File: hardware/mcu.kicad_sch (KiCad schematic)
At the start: 94 parts, among them J10 PRPC006SAAN-RC, J11 PRPC004SAAN-RC, J12 SBH11-NBPC-D05-SM-BK, J13 PRPC006SAAN-RC, J14 PRPC001DAAN-RC, J15 PRPC006SAAN-RC, J16 PRPC006SAAN-RC, J17 PRPC006SAAN-RC, J18 PRPC006SAAN-RC, U6 MCP9808T-E/MC, U7 AT25SF081B-MAHB-T, U8 STM32L552CEU6, U9 TCA9554PW, Y1 ECS-160-9-37-CKM-TR3, Y2 ABS05-32.768KHZ-9-T

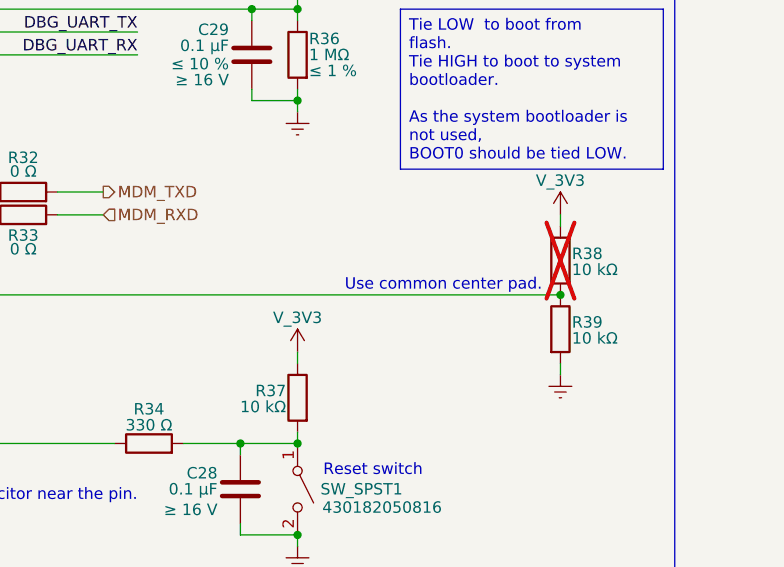
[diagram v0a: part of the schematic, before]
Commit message: HW: Increase pull-up on SIM_DET
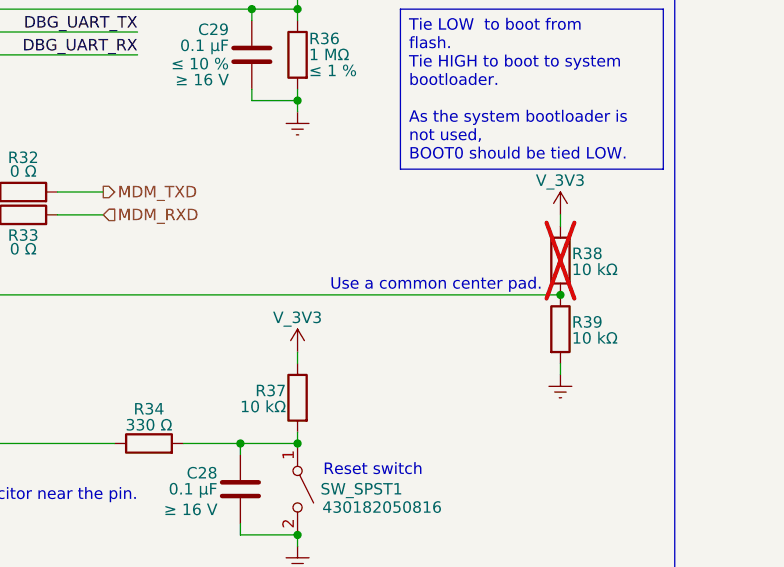
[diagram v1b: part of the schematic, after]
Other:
- note added: "Use a common center pad."
- note removed: "Use common center pad."
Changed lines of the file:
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@@
 		)
 	)
-	(text "Use common center pad."
+	(text "Use a common center pad."
 		(exclude_from_sim no)
 		(at 391.668 109.982 0)

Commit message: HW: Improve comments
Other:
- note added: "Place the GPIO headers along the edges of the PCB."
- note removed: "Place headers for GPIOs along the edges of the PCB."
- moved on the sheet: R38, R39
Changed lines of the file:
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@@
 	(text "Use a common center pad."
 		(exclude_from_sim no)
-		(at 391.668 109.982 0)
+		(at 368.808 108.712 0)
 		(effects
 			(font
@@
 		)
 	)
-	(text "Place headers for GPIOs along the edges of the PCB."
+	(text "Place the GPIO headers along the edges of the PCB."
 		(exclude_from_sim no)
 		(at 306.07 212.09 0)
@@
 		)
 	)
-	(text_box "V_BAT is at 4.2 V when fully charged.\nThis circuit draws at most\n4.2 V / 2 MΩ = 2.1 µA.\n\nV_BAT_SENSE is 2.1 V when fully charged and 1.75 V when almost empty."
+	(text_box "V_BAT is at 4.2 V when fully charged.\nThis circuit draws a maximum current of:\n4.2 V / 2 MΩ = 2.1 µA.\n\nV_BAT_SENSE is 2.1 V when fully charged and 1.75 V when nearly empty."
 		(exclude_from_sim no)
 		(at 330.2 52.07 0)
@@
 		)
 	)
-	(text_box "Tie LOW  to boot from flash.\nTie HIGH to boot to system bootloader.\n\nAs the system bootloader is not used,\nBOOT0 should be tied LOW."
+	(text_box "Connect LOW to boot from flash.\nConnect HIGH to boot to the system bootloader.\n\nSince the system bootloader is not used,\nBOOT0 should be connected to LOW."
 		(exclude_from_sim no)
-		(at 375.92 80.01 0)
-		(size 29.21 17.78)
+		(at 378.46 100.33 0)
+		(size 26.67 20.32)
 		(margins 0.9525 0.9525 0.9525 0.9525)
 		(stroke
@@
 	)
 	(junction
-		(at 393.7 111.76)
+		(at 370.84 110.49)
 		(diameter 0)
 		(color 0 0 0 0)
@@
 	(wire
 		(pts
-			(xy 393.7 120.65) (xy 393.7 119.38)
+			(xy 370.84 119.38) (xy 370.84 118.11)
 		)
 		(stroke
@@
 	(wire
 		(pts
-			(xy 393.7 102.87) (xy 393.7 104.14)
+			(xy 370.84 101.6) (xy 370.84 102.87)
 		)
 		(stroke
@@
 	(wire
 		(pts
-			(xy 330.2 111.76) (xy 393.7 111.76)
+			(xy 330.2 110.49) (xy 370.84 110.49)
 		)
 		(stroke
@@
 	(wire
 		(pts
-			(xy 330.2 111.76) (xy 330.2 125.73)
+			(xy 330.2 110.49) (xy 330.2 125.73)
 		)
 		(stroke
@@
 	(symbol
 		(lib_id "Device:R")
-		(at 393.7 115.57 0)
+		(at 370.84 114.3 0)
 		(unit 1)
 		(exclude_from_sim no)
@@
 		(dnp no)
 		(property "Reference" "R39"
-			(at 394.97 114.808 0)
+			(at 372.11 113.538 0)
 			(effects
 				(font
@@
 		)
 		(property "Value" "10 kΩ"
-			(at 394.97 116.586 0)
+			(at 372.11 115.316 0)
 			(effects
 				(font
@@
 		)
 		(property "Footprint" "Resistor_SMD:R_0402_1005Metric"
-			(at 391.922 115.57 90)
+			(at 369.062 114.3 90)
 			(effects
 				(font
@@
 		)
 		(property "Datasheet" "~"
-			(at 393.7 115.57 0)
+			(at 370.84 114.3 0)
 			(effects
 				(font
@@
 		)
 		(property "Description" ""
-			(at 393.7 115.57 0)
+			(at 370.84 114.3 0)
 			(effects
 				(font
@@
 		)
 		(property "Manufacturer" "Würth Elektronik"
-			(at 393.7 115.57 0)
+			(at 370.84 114.3 0)
 			(effects
 				(font
@@
 		)
 		(property "MPN" "560112110020"
-			(at 393.7 115.57 0)
+			(at 370.84 114.3 0)
 			(effects
 				(font
@@
 		)
 		(property "DigiKey Part Number" "732-560112110020CT-ND"
-			(at 393.7 115.57 0)
+			(at 370.84 114.3 0)
 			(effects
 				(font
@@
 		)
 		(property "Footprint review check" "+"
-			(at 393.7 115.57 0)
+			(at 370.84 114.3 0)
 			(effects
 				(font
@@
 		)
 		(property "Tolerance" "≤ 5 %"
-			(at 394.97 117.348 0)
+			(at 372.11 116.078 0)
 			(effects
 				(font
@@
 	(symbol
 		(lib_id "power:Earth")
-		(at 393.7 120.65 0)
+		(at 370.84 119.38 0)
 		(unit 1)
 		(exclude_from_sim no)
@@
 		(fields_autoplaced yes)
 		(property "Reference" "#PWR086"
-			(at 393.7 127 0)
+			(at 370.84 125.73 0)
 			(effects
 				(font
@@
 		)
 		(property "Value" "GND"
-			(at 393.7 125.73 0)
+			(at 370.84 124.46 0)
 			(effects
 				(font
@@
 		)
 		(property "Footprint" ""
-			(at 393.7 120.65 0)
+			(at 370.84 119.38 0)
 			(effects
 				(font
@@
 		)
 		(property "Datasheet" "~"
-			(at 393.7 120.65 0)
+			(at 370.84 119.38 0)
 			(effects
 				(font
@@
 		)
 		(property "Description" "Power symbol creates a global label with name \"Earth\""
-			(at 393.7 120.65 0)
+			(at 370.84 119.38 0)
 			(effects
 				(font
@@
 	(symbol
 		(lib_id "power:+3.3V")
-		(at 393.7 102.87 0)
+		(at 370.84 101.6 0)
 		(unit 1)
 		(exclude_from_sim no)
@@
 		(dnp no)
 		(property "Reference" "#PWR085"
-			(at 393.7 106.68 0)
+			(at 370.84 105.41 0)
 			(effects
 				(font
@@
 		)
 		(property "Value" "V_3V3"
-			(at 393.7 99.06 0)
+			(at 370.84 97.79 0)
 			(effects
 				(font
@@
 		)
 		(property "Footprint" ""
-			(at 393.7 102.87 0)
+			(at 370.84 101.6 0)
 			(effects
 				(font
@@
 		)
 		(property "Datasheet" ""
-			(at 393.7 102.87 0)
+			(at 370.84 101.6 0)
 			(effects
 				(font
@@
 		)
 		(property "Description" "Power symbol creates a global label with name \"+3.3V\""
-			(at 393.7 102.87 0)
+			(at 370.84 101.6 0)
 			(effects
 				(font
@@
 	(symbol
 		(lib_id "Device:R")
-		(at 393.7 107.95 0)
+		(at 370.84 106.68 0)
 		(unit 1)
 		(exclude_from_sim no)
@@
 		(dnp yes)
 		(property "Reference" "R38"
-			(at 394.97 107.188 0)
+			(at 372.11 105.918 0)
 			(effects
 				(font
@@
 		)
 		(property "Value" "10 kΩ"
-			(at 394.97 108.966 0)
+			(at 372.11 107.696 0)
 			(effects
 				(font
@@
 		)
 		(property "Footprint" "Resistor_SMD:R_0402_1005Metric"
-			(at 391.922 107.95 90)
+			(at 369.062 106.68 90)
 			(effects
 				(font
@@
 		)
 		(property "Datasheet" "~"
-			(at 393.7 107.95 0)
+			(at 370.84 106.68 0)
 			(effects
 				(font
@@
 		)
 		(property "Description" ""
-			(at 393.7 107.95 0)
+			(at 370.84 106.68 0)
 			(effects
 				(font
@@
 		)
 		(property "Manufacturer" "Würth Elektronik"
-			(at 393.7 107.95 0)
+			(at 370.84 106.68 0)
 			(effects
 				(font
@@
 		)
 		(property "MPN" "560112110020"
-			(at 393.7 107.95 0)
+			(at 370.84 106.68 0)
 			(effects
 				(font
@@
 		)
 		(property "DigiKey Part Number" "732-560112110020CT-ND"
-			(at 393.7 107.95 0)
+			(at 370.84 106.68 0)
 			(effects
 				(font
@@
 		)
 		(property "Footprint review check" "+"
-			(at 393.7 107.95 0)
+			(at 370.84 106.68 0)
 			(effects
 				(font
@@
 		)
 		(property "Tolerance" "≤ 5 %"
-			(at 394.97 109.728 0)
+			(at 372.11 108.458 0)
 			(effects
 				(font

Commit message: HW: Add battery monitoring with MAX17048
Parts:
- removed C29: 0.1 µF, Capacitor_SMD:C_0402_1005Metric, symbol Device:C
- removed R30, R31: 0 Ω, Resistor_SMD:R_0402_1005Metric, symbol Device:R
- removed R35, R36: 1 MΩ, Resistor_SMD:R_0402_1005Metric, symbol Device:R
- removed TP21: TestPoint, TestPoint:TestPoint_Pad_D1.0mm, symbol Connector:TestPoint
- added R20: 10 kΩ, Resistor_SMD:R_0402_1005Metric, symbol Device:R
- added R24, R32, R33: 0 Ω, Resistor_SMD:R_0402_1005Metric, symbol Device:R
- renumbered C13 to C14, C14 to C15, C15 to C16, C16 to C17, C17 to C18, C18 to C19, C19 to C20, C20 to C21, C21 to C23, C23 to C24, C24 to C25, C25 to C26, C26 to C27, C27 to C28, C28 to C29, R22 to R18, R21 to R19, R18 to R21, R19 to R22, R20 to R23, R23 to R25, R24 to R26, R25 to R27, R26 to R28, R27 to R29, R28 to R30, R29 to R31, R32 to R34, R33 to R35, R34 to R36, TP20 to TP21, U9 to U10, U6 to U7, U7 to U8, U8 to U9
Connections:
- net V_BAT_SENSE is gone; now on net GPIO_PA1: U9.11 (PA1)
- net DBG_UART_RX: now also R33.2
- net DBG_UART_TX: now also R32.2
- net V_3V3: now also R20.1
- net GPIO_PA1: now reaches J18.5 (Pin_5)
- net at U9.12 (PA2): now also R32.1
- net at U9.13 (PA3): now also R33.1
- net at U10.12 (P7): now also R24.2
- new net BAT_INT: R20.2, R24.1
- no-connect marks 10 -> 8
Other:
- moved on the sheet: C23, R18, R19, R21, R22, R23, R38, R39, U10

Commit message: HW: Reorganize schematic
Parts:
- removed C15: 0.1 µF, Capacitor_SMD:C_0402_1005Metric, symbol Device:C
- removed C25, C26, C27, C28: 8 pF, Capacitor_SMD:C_0402_1005Metric, symbol Device:C
- removed J11: PRPC004SAAN-RC, Connector_PinHeader_2.54mm:PinHeader_1x04_P2.54mm_Vertical, symbol Connector_Generic:Conn_01x04
- removed J14: PRPC001DAAN-RC, Connector_PinHeader_2.54mm:PinHeader_1x02_P2.54mm_Vertical, symbol Connector_Generic:Conn_01x02
- removed LED6, LED7, LED8: 150141RS73100, LED_SMD:LED_PLCC_2835, symbol Device:LED
- removed R18: 4.7 kΩ, Resistor_SMD:R_0402_1005Metric, symbol Device:R
- removed R20: 10 kΩ, Resistor_SMD:R_0402_1005Metric, symbol Device:R
- removed R21, R22, R23, R24, R32, R33, R34, R35: 0 Ω, Resistor_SMD:R_0402_1005Metric, symbol Device:R
- removed R25: 2.2 kΩ, Resistor_SMD:R_0402_1005Metric, symbol Device:R
- removed TP22, TP23, TP24, TP25, TP26, TP27, TP28, TP29, TP30, TP31, TP32, TP33, TP34, TP35, TP36, TP37, TP38, TP39, TP40, TP41, TP42, TP43, TP44, TP45, TP46, TP47, TP48, TP49: TestPoint, TestPoint:TestPoint_Pad_D1.0mm, symbol Connector:TestPoint
- removed U10: TCA9554PW, Package_SO:TSSOP-16_4.4x5mm_P0.65mm, symbol Interface_Expansion:TCA9554PW
- removed U7: MCP9808T-E/MC, Package_DFN_QFN:DFN-8-1EP_3x2mm_P0.5mm_EP1.75x1.45mm, symbol MCP9808:MCP9808T-E/MC
- added C18, C19, C24: 8 pF, Capacitor_SMD:C_0402_1005Metric, symbol Device:C
- added J16: PRPC006SAAN-RC, Connector_PinHeader_2.54mm:PinHeader_1x06_P2.54mm_Vertical, symbol Connector_Generic:Conn_01x06
- added J18: PRPC001DAAN-RC, Connector_PinHeader_2.54mm:PinHeader_1x02_P2.54mm_Vertical, symbol Connector_Generic:Conn_01x02
- added R28, R29: 0 Ω, Resistor_SMD:R_0402_1005Metric, symbol Device:R
- added R31: 4.7 kΩ, Resistor_SMD:R_0402_1005Metric, symbol Device:R
- C23: value 0.1 µF -> 8 pF; Class X7R -> C0G; DigiKey Part Number 490-7998-1-ND -> 490-3109-1-ND; MPN GCM155R71C104KA55J -> GJM1555C1H8R0CB01D; Tolerance ≤ 10 % -> ≤ 1 %; Voltage ≥ 16 V -> ≥ 10 V
- R26, R27: value 2.2 kΩ -> 0 Ω; DigiKey Part Number 732-560112110087CT-ND -> 732-560112110001CT-ND; MPN 560112110087 -> 560112110001; Size (none) -> 0402; Tolerance ≤ 5 % -> (none)
- U7: renamed from U9; Digi-Key Part Number (none) -> 497-STM32L552CEU6-ND
- renumbered C29 to C14, C16 to C15, C17 to C16, C18 to C17, C19 to C20, C20 to C21, C21 to C22, C22 to C25, C24 to C26, C14 to C27, J13 to J10, J12 to J11, J15 to J12, J16 to J13, J17 to J14, J18 to J15, J10 to J17, R30 to R18, R31 to R19, R28 to R20, R29 to R21, R37 to R22, R38 to R23, R39 to R24, R36 to R25, R19 to R30
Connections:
- net LED_B is gone; now on net DBG_UART_RX: R26.2
- net LED_C is gone; now on net DBG_UART_TX: R27.2
- net TEMP_INT is gone; now on net EXT_FLASH_IO2: U7.43 (PB7)
- net DBG_GPIO: now also J18.1 (Pin_1); no longer J15.3 (Pin_3)
- net EXT_FLASH_IO2: no longer U7.17 (PA7)
- net GND: now also C18.2, C19.2, C24.2, J16.2 (Pin_2), J16.4 (Pin_4), J16.6 (Pin_6), J18.2 (Pin_2)
- net I2C_SCL: now also J16.5 (Pin_5)
- net I2C_SDA: now also J16.3 (Pin_3), R31.2
- net MDM_RXD: now also R29.2
- net MDM_TXD: now also R28.2
- net OSC16M_IN: now also C18.1
- net OSC16M_OUT: now also C19.1
- net OSC32K_IN: now also C23.1
- net OSC32K_OUT: now also C24.1
- net V_3V3: now also J16.1 (Pin_1), R31.1; no longer C23.1
- net at U7.12 (PA2): now also R27.1
- net at U7.13 (PA3): now also R26.1
- net at U7.30 (PA9): now also R28.1
- net at U7.31 (PA10): now also R29.1
- net DBG_SWCLK renamed DEBUG_SWCLK
- net DBG_SWDIO renamed DEBUG_SWDIO
- net DBG_SWO renamed DEBUG_SWO
- new net GPIO_PA7: J15.3 (Pin_3), U7.17 (PA7)
- no-connect marks 8 -> 7
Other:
- note added: "Testing: Remove when functionality verified."
- note removed: "IO expander"
- note removed: "Indicator LEDs"
- note removed: "Temperature sensor"
- moved on the sheet: C14, C15, C16, C17, C20, C21, C22, C25, C26, C27, D1, D2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

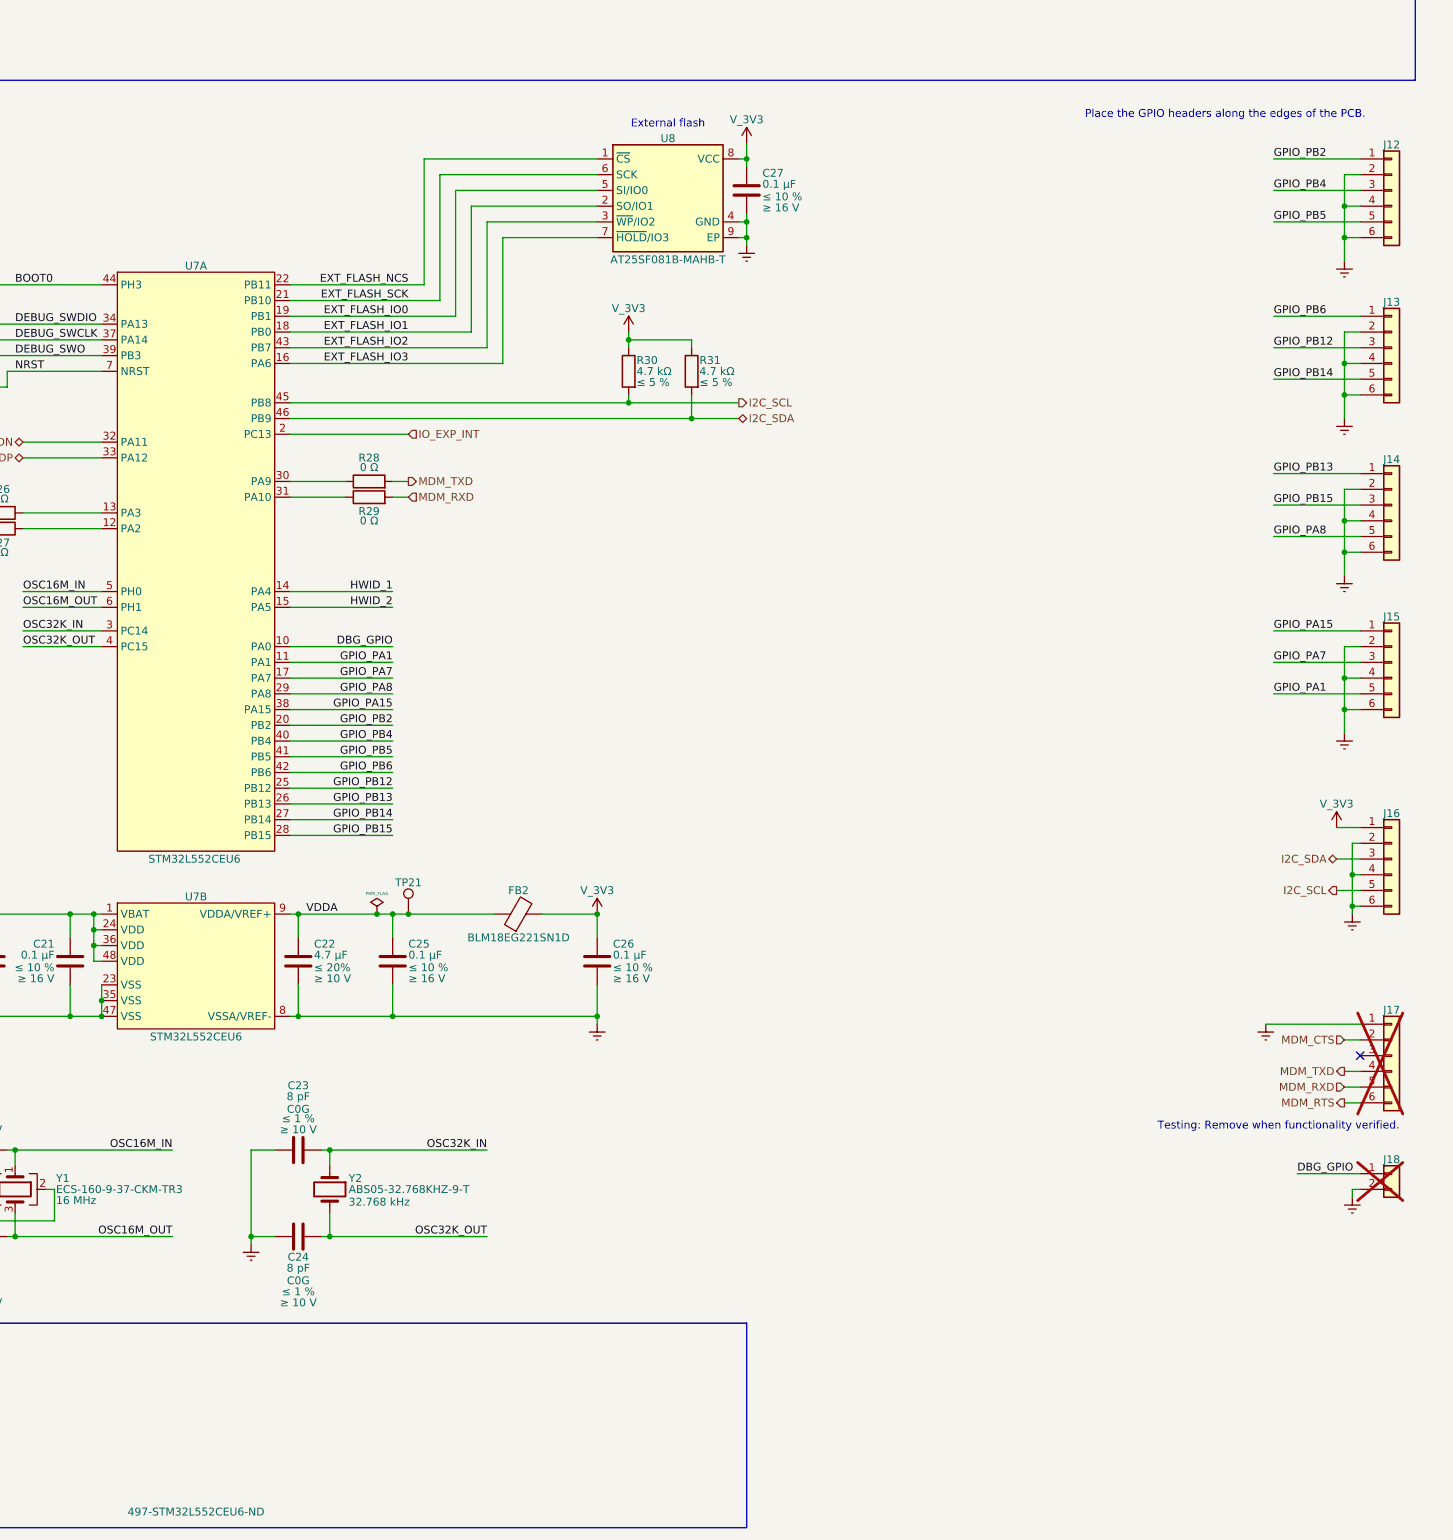
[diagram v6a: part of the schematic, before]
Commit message: HW: Fix MCU pins
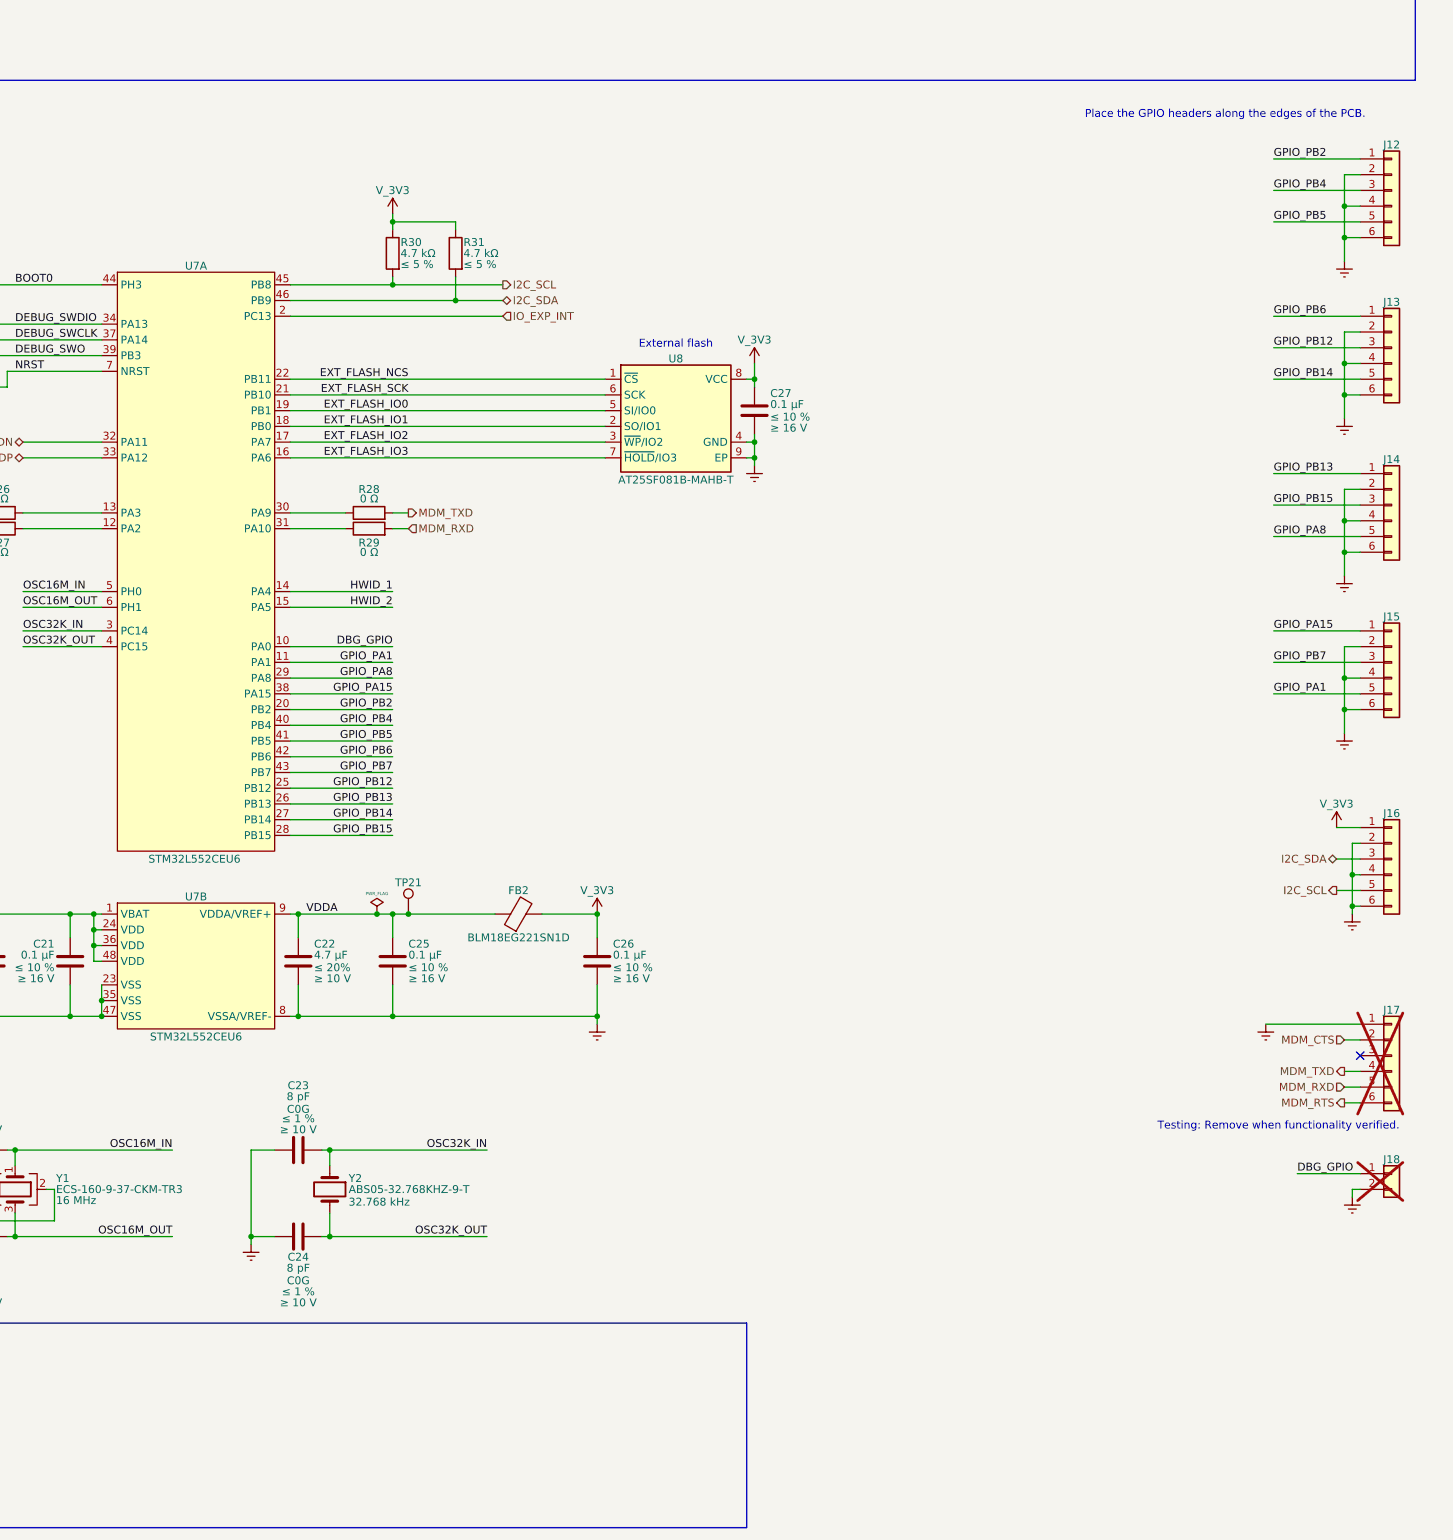
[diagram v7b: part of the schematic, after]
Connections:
- net EXT_FLASH_IO2: now also U7.17 (PA7); no longer U7.43 (PB7)
- net GPIO_PA7 renamed GPIO_PB7
- net GPIO_PB7: now also U7.43 (PB7); no longer U7.17 (PA7)
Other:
- moved on the sheet: C27, R28, R29, R30, R31, U8
